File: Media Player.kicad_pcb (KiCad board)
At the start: 2 copper layers, 142 parts, among them IC2 LM66200DRLR, J1 PH2.0, J2 MEM2075-00-140-01-A, J3 USB_C_Receptacle_USB2.0_16P, J4 UART, J6 SJ-3524-SMT-TR, Q1 DMP3068L-7, Q2 DMP3068L-7, Q3 DMP3068L-7, Q5 DMP3068L-7, SW1 BOOT, SW2 RESET, SW3 SW_Push, SW4 SW_Push, SW5 SW_Push, SW6 SW_Push, SW7 SW_SPST, SW8 SW_SPST, U1 ESP32-S3-WROOM-1, U3 MIC845H, U4 TPS631000DRLR, U5 MCP73831-2-OT, U6 WM8731SEDS

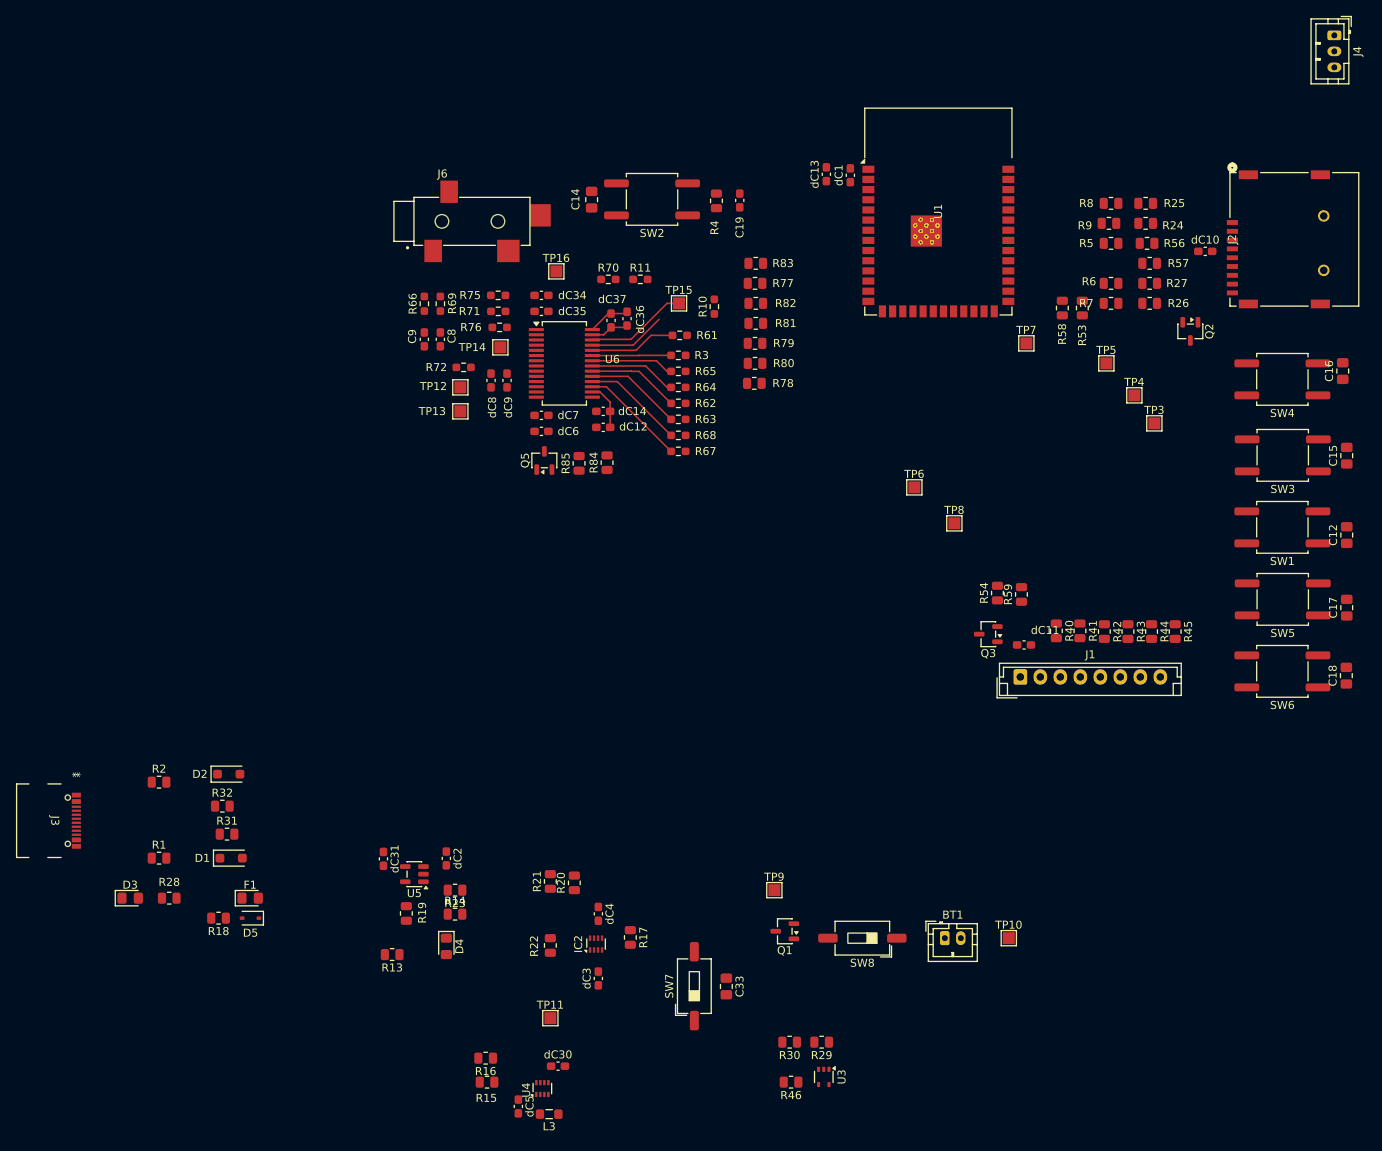
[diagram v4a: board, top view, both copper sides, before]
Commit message: Draft 1
I'm not very fond of some of my traces. Especially the power component. Not even sure if all components are routed properly. Still missing GND and PWR plane, so most component power not routed. Missing LCD screw holes. Power and signal traces are using same width/thickness, and also have not checked with what JLC allows during fabrication. I should try again, working from general (blocking) to specifics (details), much like how I started with schematics. Many conventions I have not learned.
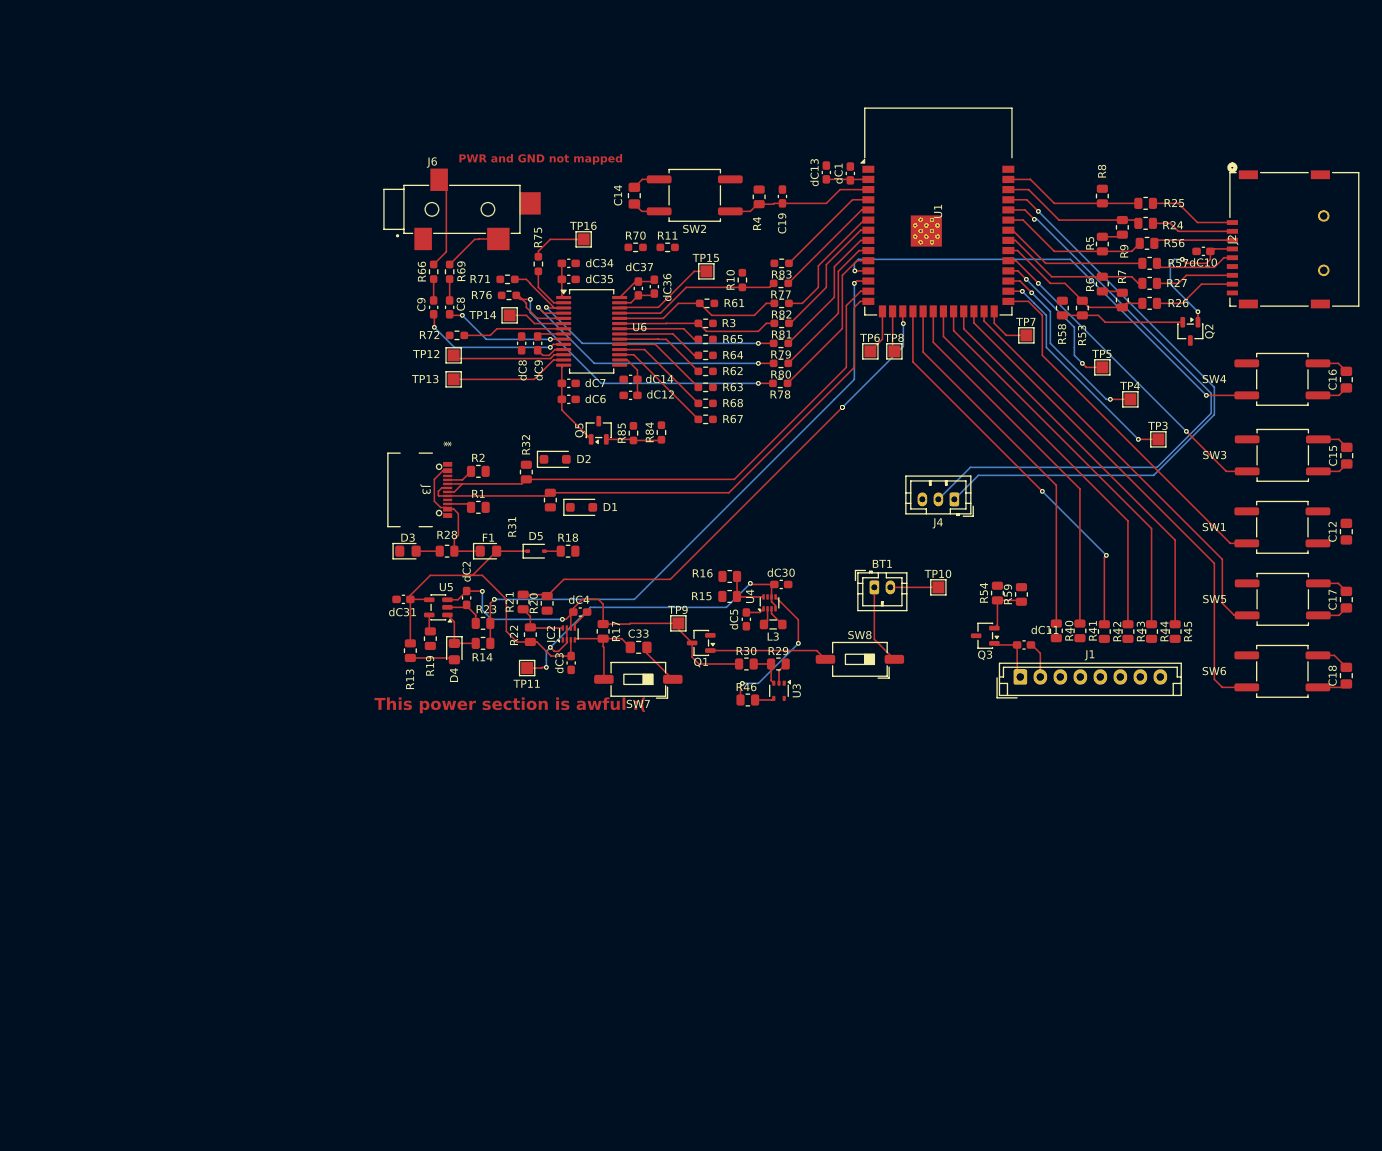
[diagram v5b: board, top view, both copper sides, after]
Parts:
- R77, R78, R79, R80, R81, R82, R83, R84, R85: footprint Resistor_SMD:R_0805_2012Metric -> Resistor_SMD:R_0603_1608Metric_Pad0.98x0.95mm_HandSolder
- moved J4 75.0 mm to (148.0, 93.0), turned to 180 degrees
- moved R15 67.9 mm to (119.9, 105.1)
- moved R16 67.5 mm to (119.9, 102.6)
- moved L3 67.3 mm to (125.3, 108.6)
- moved dC5 67.2 mm to (122.0, 108.0)
- moved U4 67.0 mm to (124.9, 105.9)
- moved dC30 66.4 mm to (126.4, 103.6)
- moved R18 63.3 mm to (99.7, 99.5), turned to 0 degrees
- moved J3 62.2 mm to (81.0, 91.8)
- moved D1 62.0 mm to (101.4, 94.0)
- moved R1 59.3 mm to (88.5, 94.0)
- moved D5 58.1 mm to (95.7, 99.5), turned to 0 degrees
- moved R31 58.1 mm to (97.5, 93.1), turned to 90 degrees
- moved D2 56.7 mm to (98.1, 88.0)
- moved R32 56.5 mm to (94.5, 89.6), turned to -90 degrees
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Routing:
- net /CHRG_STAT: track 0.00 -> 76.0 mm, vias 0 -> 2
- net /RXD0: track 0.00 -> 75.9 mm, vias 0 -> 1
- net /TXD0: track 0.00 -> 75.8 mm, vias 0 -> 1
- net /USB_D+: track 0.00 -> 70.1 mm
- net /USB_D-: track 0.00 -> 69.3 mm
- net /PB3: track 0.00 -> 66.6 mm
- net /PWR_SRC: track 0.00 -> 64.9 mm, vias 0 -> 3
- net /PB1: track 0.00 -> 62.9 mm, vias 0 -> 2
- net /PB2: track 0.00 -> 56.4 mm
- net /LCD_BL: track 0.00 -> 50.1 mm
- net GND: track 5.26 -> 55.2 mm
- net VBAT: track 0.00 -> 49.5 mm, vias 0 -> 2
- net /LCD_RST_n: track 0.00 -> 49.4 mm
- net /LCD_CS_n: track 0.00 -> 49.2 mm, vias 0 -> 2
- net /LCD_DS: track 0.00 -> 48.7 mm
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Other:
- board text added: "PWR and GND not mapped"
- board text added: "This power section is awful :("

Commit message: Temporary Commit
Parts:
- moved Q3 62.9 mm to (96.6, 79.9)
- moved C14 62.9 mm to (52.8, 24.9)
- moved C19 62.9 mm to (71.3, 25.0)
- moved D1 62.9 mm to (46.1, 63.9)
- moved D4 62.9 mm to (30.2, 81.9)
- moved D5 62.9 mm to (40.5, 69.3)
- moved J1 62.9 mm to (101.0, 85.1)
- moved J4 62.9 mm to (92.8, 62.9)
- moved L3 62.9 mm to (70.1, 78.5)
- moved Q1 62.9 mm to (61.1, 80.8)
- moved Q2 62.9 mm to (122.2, 41.9)
- moved R1 62.9 mm to (33.2, 63.9)
- moved R10 62.9 mm to (66.2, 35.5)
- moved R14 62.9 mm to (33.8, 80.9)
- moved R15 62.9 mm to (64.7, 75.0)
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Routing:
- net /CHRG_STAT: track 76.0 -> 0.00 mm, vias 2 -> 0
- net /RXD0: track 75.9 -> 0.00 mm, vias 1 -> 0
- net /TXD0: track 75.8 -> 0.00 mm, vias 1 -> 0
- net /USB_D+: track 70.1 -> 0.00 mm
- net /USB_D-: track 69.3 -> 0.00 mm
- net /PB3: track 66.6 -> 0.00 mm
- net /PWR_SRC: track 64.9 -> 0.00 mm, vias 3 -> 0
- net /PB1: track 62.9 -> 0.00 mm, vias 2 -> 0
- net /PB2: track 56.4 -> 0.00 mm
- net GND: track 55.2 -> 0.00 mm
- net /LCD_BL: track 50.1 -> 0.00 mm
- net VBAT: track 49.5 -> 0.00 mm, vias 2 -> 0
- net /LCD_RST_n: track 49.4 -> 0.00 mm
- net /LCD_CS_n: track 49.2 -> 0.00 mm, vias 2 -> 0
- net /LCD_DS: track 48.7 -> 0.00 mm
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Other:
- copper layers 2 -> 4

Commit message: Compacting part 1
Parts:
- removed R28: 5.1k, Resistor_SMD:R_0805_2012Metric
- removed R31, R32: 0Ω, Resistor_SMD:R_0805_2012Metric
- removed the R70 at (52.9, 31.4)
- added C0: 10uF, Capacitor_SMD:C_0805_2012Metric_Pad1.18x1.45mm_HandSolder, F.Cu at (59.6, 70.0)
- added D0: 1N5819HW-7-F, Diode_SMD:D_SOD-123, F.Cu at (54.3, 70.2)
- added D51: RED, LED_SMD:LED_0603_1608Metric, F.Cu at (66.0, 63.7)
- added R63: 5.1kΩ, Resistor_SMD:R_0805_2012Metric, F.Cu at (66.2, 60.9)
- D1, D2: value SMF3.3 -> LESD5D5.0CT1G; footprint Diode_SMD:D_SOD-123F -> Diode_SMD:D_SMA
- D3: value GG0402055R042P -> LESD5D5.0CT1G; footprint Diode_SMD:D_0805_2012Metric_Pad1.15x1.40mm_HandSolder -> Diode_SMD:D_SMA
- moved D3 31.1 mm to (55.4, 66.2)
- moved R1 12.1 mm to (23.9, 71.5), turned to -90 degrees
- moved R85 11.3 mm to (45.7, 30.0)
- moved R2 9.54 mm to (24.1, 56.7), turned to 90 degrees
- moved R23 8.97 mm to (115.2, 39.5)
- moved D1 7.51 mm to (39.5, 67.4), turned to -90 degrees
- moved R13 7.27 mm to (106.8, 35.8), turned to 180 degrees
- moved R15 7.14 mm to (106.8, 27.2), turned to 180 degrees
- moved R89 6.81 mm to (70.6, 41.6)
- moved C80 6.30 mm to (28.8, 45.1)
- moved C81 6.25 mm to (27.3, 45.1)
- moved R75 6.18 mm to (36.5, 44.2)
- moved TP72 6.08 mm to (36.1, 46.2)
- moved TP73 5.99 mm to (36.1, 48.7)
- moved R91 5.82 mm to (70.6, 40.1)
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- renumbered BT1 to BT50, dC13 to C1, dC10 to C10, dC1 to C2, C19 to C3, C12 to C30, C14 to C31, C15 to C32, C16 to C33, C17 to C34, C18 to C35, C33 to C36, dC11 to C40, dC31 to C50, dC2 to C51, dC3 to C52, dC4 to C53, dC30 to C54, dC5 to C55, dC6 to C70, dC7 to C71, dC8 to C72, dC9 to C73, dC36 to C74, dC37 to C75, dC34 to C76, dC35 to C77, dC12 to C78, dC14 to C79, C8 to C80, C9 to C81, D5 to D4, D4 to D50, F1 to F0, J3 to J1, J2 to J10, J1 to J40, J4 to J41, J6 to J70, L3 to L50, Q2 to Q10, Q3 to Q40, Q1 to Q50, Q5 to Q70, R18 to R0, R5 to R11, R6 to R12, R7 to R13, R8 to R14, R9 to R15, R24 to R16, R25 to R17, R26 to R18, R27 to R19, R56 to R20, R57 to R21, R53 to R22, R58 to R23, R4 to R3, R59 to R47, R54 to R48, R19 to R50, R14 to R51, R23 to R52, R13 to R53, R30 to R54, R29 to R55, R46 to R56, R17 to R57, R22 to R58, R21 to R59, R20 to R60, R16 to R61, R15 to R62, R61 to R70, R3 to R71, R65 to R72, R64 to R73, R76 to R74, R72 to R75, R71 to R76, R10 to R77, R75 to R78, R62 to R79, R63 to R80, R67 to R81, R68 to R82, R69 to R83, R66 to R84, R11 to R85, R81 to R86, R82 to R87, R77 to R88, R78 to R89, R79 to R90, R80 to R91, R83 to R92, R84 to R93, R85 to R94, SW1 to SW30, SW2 to SW31, SW3 to SW32, SW4 to SW33, SW5 to SW34, SW6 to SW35, SW7 to SW36, SW8 to SW50, TP9 to TP50, TP10 to TP51, TP11 to TP52, TP16 to TP70, TP15 to TP71, TP12 to TP72, TP13 to TP73, U5 to U50, U3 to U51, IC2 to U52, U4 to U53, U6 to U70
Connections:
- D1 pad 1: Net-(D1-A1) -> /USB_D+
- D2 pad 1: Net-(D2-A1) -> /USB_D-
- D3 pad 1: GND -> Net-(D0-K)
- D3 pad 2: Net-(D3-A2) -> GND
- F0 pad 1: Net-(F1-Pad1) -> Net-(D0-K)
- J1 pad A4: Net-(F1-Pad1) -> Net-(D0-A)
- J1 pad B4: Net-(F1-Pad1) -> Net-(D0-A)
- J70 pad TN: Net-(J6-PadTN) -> /AudioAlt/A2_TSW
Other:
- board text added: "The PTC fuse diode pads are too small! Recall, this to support high amounts of current"
- board text added: "These TVS are huge! Return to original component!"

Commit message: Compacting Part 2, Pre-Draft 2
Compacted more parts. Organized power routing and added envisioned power plane sections. Added screw holes for board and LCD. Shrunk max board size down.

Still need to replace the diode for surge prot as the copper pads are way too small for direction large amounts of current.
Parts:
- moved TP50 83.0 mm to (140.2, 97.2)
- moved Q50 81.0 mm to (140.2, 102.5), turned to 90 degrees
- moved F0 75.4 mm to (109.3, 84.2)
- moved D4 73.5 mm to (113.1, 84.2)
- moved R0 73.3 mm to (117.2, 84.2)
- moved TP52 72.8 mm to (112.3, 93.2), turned to 180 degrees
- moved R59 72.4 mm to (109.0, 97.6), turned to 0 degrees
- moved C50 70.6 mm to (93.8, 90.2), turned to -90 degrees
- moved R58 70.1 mm to (109.0, 95.7), turned to 180 degrees
- moved R60 70.0 mm to (109.0, 99.5), turned to 0 degrees
- moved D51 69.7 mm to (129.2, 93.2), turned to -90 degrees
- moved R54 69.6 mm to (135.9, 97.2), turned to 0 degrees
- moved R63 69.1 mm to (127.2, 93.1), turned to -90 degrees
- moved R2 68.0 mm to (90.8, 69.7), turned to 180 degrees
- moved R1 67.9 mm to (90.9, 82.5), turned to 180 degrees
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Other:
- board outline added: 114.3 x 68.5 mm
- board text added: "3.7V Area"
- board text added: "5V Area"
- board text added: "ADC"
- board text added: "BOOT"
- board text added: "CLKOUT"
- board text added: "GND"
- board text added: "GPIO3"
- board text added: "GPIO35"
- board text added: "GPIO36"
- board text added: "GPIO37"
- board text added: "GPIO45"
- board text added: "GPIO46"
- board text added: "LOUT"
- board text added: "RESET"
- board text added: "ROUT"
- board text added: "VBAT"
- board text added: "VSRC"
- board text added: "XTO"
- board text removed: "This power section is awful :("
